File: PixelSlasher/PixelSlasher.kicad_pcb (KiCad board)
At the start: 2 copper layers, 52.8 x 149.3 mm, 22 parts, among them J1 VGA Input, J2 CV Red, J3 CV Green, J4 CV Blue, Q1 BC337, Q2 BC337, Q3 BC337, SW1 SW_SPDT, SW2 SW_SPDT, SW3 SW_SPDT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

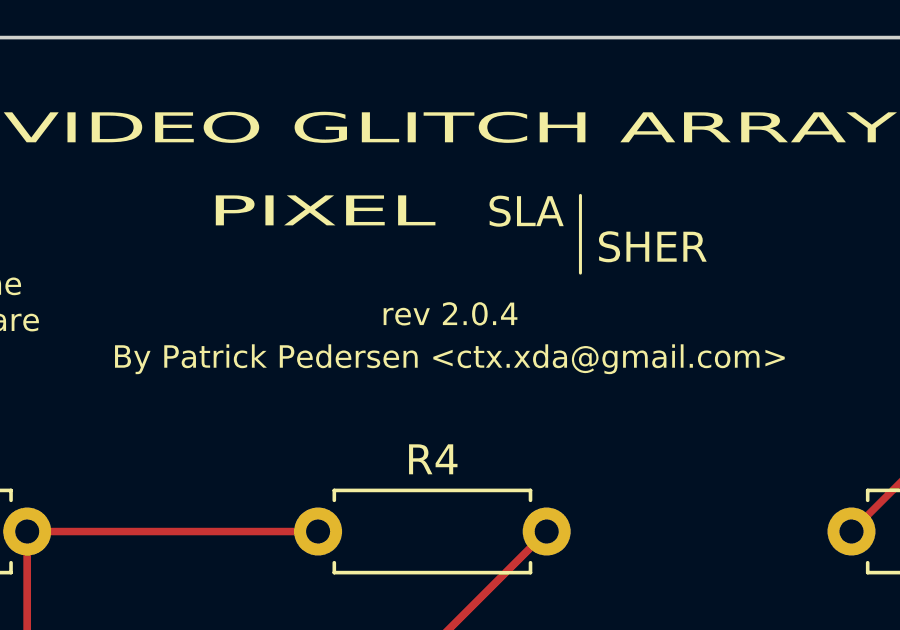
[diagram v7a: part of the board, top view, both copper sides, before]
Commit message: PixelSlasher: Rev 2.0.5: Ground slide pot case mounts
Signed-off-by: Patrick Pedersen <ctx.xda@gmail.com>
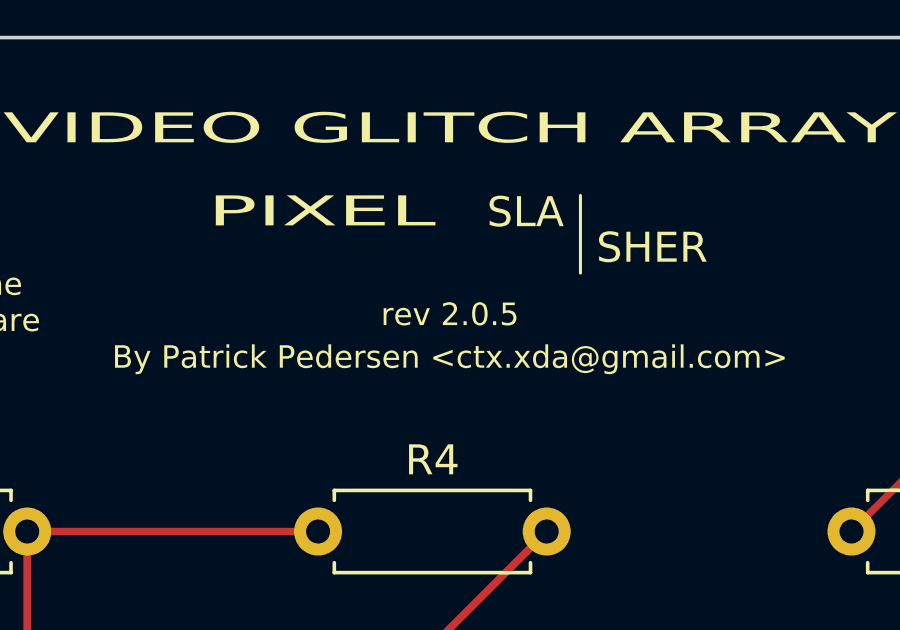
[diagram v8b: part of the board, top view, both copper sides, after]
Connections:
- RV1 pad MP: (no net) -> GND
- RV2 pad MP: (no net) -> GND
- RV3 pad MP: (no net) -> GND
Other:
- board text added: "rev 2.0.5"
- board text removed: "rev 2.0.4"
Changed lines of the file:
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@@
   (title_block
     (date 2019-08-30)
-    (rev 2.0.4)
+    (rev 2.0.5)
     (comment 2 https://www.tapr.org/ohl.html)
     (comment 3 "License: TAPR Open Hardware License v1.0")
@@
     (mod_text_size 1 1)
     (mod_text_width 0.15)
-    (pad_size 1.524 1.524)
-    (pad_drill 0.762)
+    (pad_size 2.7 2.7)
+    (pad_drill 1.7)
     (pad_to_mask_clearance 0.051)
     (solder_mask_min_width 0.25)
@@
       (effects (font (size 1 1) (thickness 0.15)))
     )
+    (fp_text user %R (at 29.25 1.75 90) (layer F.Fab)
+      (effects (font (size 1 1) (thickness 0.15)))
+    )
+    (fp_line (start 59.75 -3.25) (end -1.25 -3.25) (layer F.CrtYd) (width 0.05))
+    (fp_line (start 59.75 6.75) (end 59.75 -3.25) (layer F.CrtYd) (width 0.05))
+    (fp_line (start -1.25 6.75) (end 59.75 6.75) (layer F.CrtYd) (width 0.05))
+    (fp_line (start -1.25 -3.25) (end -1.25 6.75) (layer F.CrtYd) (width 0.05))
+    (fp_line (start 51.75 1.75) (end 51 2.5) (layer F.SilkS) (width 0.12))
+    (fp_line (start 51 1) (end 51.75 1.75) (layer F.SilkS) (width 0.12))
+    (fp_line (start 51.75 0.25) (end 51.75 3.25) (layer F.SilkS) (width 0.12))
+    (fp_line (start 6.75 1.75) (end 7.5 2.5) (layer F.SilkS) (width 0.12))
+    (fp_line (start 7.5 1) (end 6.75 1.75) (layer F.SilkS) (width 0.12))
+    (fp_line (start 6.75 0.25) (end 6.75 3.25) (layer F.SilkS) (width 0.12))
+    (fp_line (start 6.75 1.75) (end 51.75 1.75) (layer F.SilkS) (width 0.12))
+    (fp_line (start -1.675 0.5) (end -1.175 0) (layer F.SilkS) (width 0.12))
+    (fp_line (start -1.675 -0.5) (end -1.675 0.5) (layer F.SilkS) (width 0.12))
+    (fp_line (start -1.175 0) (end -1.675 -0.5) (layer F.SilkS) (width 0.12))
+    (fp_line (start 59.37 0.823) (end 59.37 6.37) (layer F.SilkS) (width 0.12))
+    (fp_line (start 59.37 -2.87) (end 59.37 -0.823) (layer F.SilkS) (width 0.12))
+    (fp_line (start -0.87 4.323) (end -0.87 6.37) (layer F.SilkS) (width 0.12))
+    (fp_line (start -0.87 1.175) (end -0.87 2.678) (layer F.SilkS) (width 0.12))
+    (fp_line (start -0.87 -2.87) (end -0.87 -1.175) (layer F.SilkS) (width 0.12))
+    (fp_line (start 55.986 6.37) (end 59.37 6.37) (layer F.SilkS) (width 0.12))
+    (fp_line (start 5.786 6.37) (end 52.715 6.37) (layer F.SilkS) (width 0.12))
+    (fp_line (start -0.87 6.37) (end 2.515 6.37) (layer F.SilkS) (width 0.12))
+    (fp_line (start 54.786 -2.87) (end 59.37 -2.87) (layer F.SilkS) (width 0.12))
+    (fp_line (start 6.986 -2.87) (end 51.515 -2.87) (layer F.SilkS) (width 0.12))
+    (fp_line (start -0.87 -2.87) (end 3.715 -2.87) (layer F.SilkS) (width 0.12))
+    (fp_line (start -0.75 -1.75) (end 0.25 -2.75) (layer F.Fab) (width 0.1))
+    (fp_line (start -0.75 6.25) (end -0.75 -1.75) (layer F.Fab) (width 0.1))
+    (fp_line (start 59.25 6.25) (end -0.75 6.25) (layer F.Fab) (width 0.1))
+    (fp_line (start 59.25 -2.75) (end 59.25 6.25) (layer F.Fab) (width 0.1))
+    (fp_line (start 0.25 -2.75) (end 59.25 -2.75) (layer F.Fab) (width 0.1))
+    (fp_circle (center 57.25 1.75) (end 58.25 1.75) (layer F.Fab) (width 0.1))
     (fp_circle (center 1.25 1.75) (end 2.25 1.75) (layer F.Fab) (width 0.1))
-    (fp_circle (center 57.25 1.75) (end 58.25 1.75) (layer F.Fab) (width 0.1))
-    (fp_line (start 0.25 -2.75) (end 59.25 -2.75) (layer F.Fab) (width 0.1))
-    (fp_line (start 59.25 -2.75) (end 59.25 6.25) (layer F.Fab) (width 0.1))
-    (fp_line (start 59.25 6.25) (end -0.75 6.25) (layer F.Fab) (width 0.1))
-    (fp_line (start -0.75 6.25) (end -0.75 -1.75) (layer F.Fab) (width 0.1))
-    (fp_line (start -0.75 -1.75) (end 0.25 -2.75) (layer F.Fab) (width 0.1))
-    (fp_line (start -0.87 -2.87) (end 3.715 -2.87) (layer F.SilkS) (width 0.12))
-    (fp_line (start 6.986 -2.87) (end 51.515 -2.87) (layer F.SilkS) (width 0.12))
-    (fp_line (start 54.786 -2.87) (end 59.37 -2.87) (layer F.SilkS) (width 0.12))
-    (fp_line (start -0.87 6.37) (end 2.515 6.37) (layer F.SilkS) (width 0.12))
-    (fp_line (start 5.786 6.37) (end 52.715 6.37) (layer F.SilkS) (width 0.12))
-    (fp_line (start 55.986 6.37) (end 59.37 6.37) (layer F.SilkS) (width 0.12))
-    (fp_line (start -0.87 -2.87) (end -0.87 -1.175) (layer F.SilkS) (width 0.12))
-    (fp_line (start -0.87 1.175) (end -0.87 2.678) (layer F.SilkS) (width 0.12))
-    (fp_line (start -0.87 4.323) (end -0.87 6.37) (layer F.SilkS) (width 0.12))
-    (fp_line (start 59.37 -2.87) (end 59.37 -0.823) (layer F.SilkS) (width 0.12))
-    (fp_line (start 59.37 0.823) (end 59.37 6.37) (layer F.SilkS) (width 0.12))
-    (fp_line (start -1.175 0) (end -1.675 -0.5) (layer F.SilkS) (width 0.12))
-    (fp_line (start -1.675 -0.5) (end -1.675 0.5) (layer F.SilkS) (width 0.12))
-    (fp_line (start -1.675 0.5) (end -1.175 0) (layer F.SilkS) (width 0.12))
-    (fp_line (start 6.75 1.75) (end 51.75 1.75) (layer F.SilkS) (width 0.12))
-    (fp_line (start 6.75 0.25) (end 6.75 3.25) (layer F.SilkS) (width 0.12))
-    (fp_line (start 7.5 1) (end 6.75 1.75) (layer F.SilkS) (width 0.12))
-    (fp_line (start 6.75 1.75) (end 7.5 2.5) (layer F.SilkS) (width 0.12))
-    (fp_line (start 51.75 0.25) (end 51.75 3.25) (layer F.SilkS) (width 0.12))
-    (fp_line (start 51 1) (end 51.75 1.75) (layer F.SilkS) (width 0.12))
-    (fp_line (start 51.75 1.75) (end 51 2.5) (layer F.SilkS) (width 0.12))
-    (fp_line (start -1.25 -3.25) (end -1.25 6.75) (layer F.CrtYd) (width 0.05))
-    (fp_line (start -1.25 6.75) (end 59.75 6.75) (layer F.CrtYd) (width 0.05))
-    (fp_line (start 59.75 6.75) (end 59.75 -3.25) (layer F.CrtYd) (width 0.05))
-    (fp_line (start 59.75 -3.25) (end -1.25 -3.25) (layer F.CrtYd) (width 0.05))
-    (fp_text user %R (at 29.25 1.75 90) (layer F.Fab)
-      (effects (font (size 1 1) (thickness 0.15)))
-    )
+    (pad MP thru_hole circle (at 54.35 5.95 90) (size 2.7 2.7) (drill 1.7) (layers *.Cu *.Mask)
+      (net 4 GND))
+    (pad MP thru_hole circle (at 4.15 5.95 90) (size 2.7 2.7) (drill 1.7) (layers *.Cu *.Mask)
+      (net 4 GND))
+    (pad MP thru_hole circle (at 53.15 -2.45 90) (size 2.7 2.7) (drill 1.7) (layers *.Cu *.Mask)
+      (net 4 GND))
+    (pad MP thru_hole circle (at 5.35 -2.45 90) (size 2.7 2.7) (drill 1.7) (layers *.Cu *.Mask)
+      (net 4 GND))
+    (pad 3 thru_hole circle (at 58.5 0 90) (size 1.75 1.75) (drill 1.2) (layers *.Cu *.Mask)
+      (net 4 GND))
+    (pad 2 thru_hole circle (at 0 3.5 90) (size 1.75 1.75) (drill 1.2) (layers *.Cu *.Mask)
+      (net 12 "Net-(RV1-Pad2)"))
     (pad 1 thru_hole rect (at 0 0 90) (size 1.75 1.75) (drill 1.2) (layers *.Cu *.Mask)
       (net 9 "Net-(R1-Pad2)"))
-    (pad 2 thru_hole circle (at 0 3.5 90) (size 1.75 1.75) (drill 1.2) (layers *.Cu *.Mask)
-      (net 12 "Net-(RV1-Pad2)"))
-    (pad 3 thru_hole circle (at 58.5 0 90) (size 1.75 1.75) (drill 1.2) (layers *.Cu *.Mask)
-      (net 4 GND))
-    (pad MP thru_hole circle (at 5.35 -2.45 90) (size 2.7 2.7) (drill 1.7) (layers *.Cu *.Mask))
-    (pad MP thru_hole circle (at 53.15 -2.45 90) (size 2.7 2.7) (drill 1.7) (layers *.Cu *.Mask))
-    (pad MP thru_hole circle (at 4.15 5.95 90) (size 2.7 2.7) (drill 1.7) (layers *.Cu *.Mask))
-    (pad MP thru_hole circle (at 54.35 5.95 90) (size 2.7 2.7) (drill 1.7) (layers *.Cu *.Mask))
     (model ${KISYS3DMOD}/Potentiometer_THT.3dshapes/Potentiometer_Bourns_PTA4543_Single_Slide.wrl
       (at (xyz 0 0 0))
@@
     (pad 3 thru_hole circle (at 58.5 0 90) (size 1.75 1.75) (drill 1.2) (layers *.Cu *.Mask)
       (net 4 GND))
-    (pad MP thru_hole circle (at 5.35 -2.45 90) (size 2.7 2.7) (drill 1.7) (layers *.Cu *.Mask))
-    (pad MP thru_hole circle (at 53.15 -2.45 90) (size 2.7 2.7) (drill 1.7) (layers *.Cu *.Mask))
-    (pad MP thru_hole circle (at 4.15 5.95 90) (size 2.7 2.7) (drill 1.7) (layers *.Cu *.Mask))
-    (pad MP thru_hole circle (at 54.35 5.95 90) (size 2.7 2.7) (drill 1.7) (layers *.Cu *.Mask))
+    (pad MP thru_hole circle (at 5.35 -2.45 90) (size 2.7 2.7) (drill 1.7) (layers *.Cu *.Mask)
+      (net 4 GND))
+    (pad MP thru_hole circle (at 53.15 -2.45 90) (size 2.7 2.7) (drill 1.7) (layers *.Cu *.Mask)
+      (net 4 GND))
+    (pad MP thru_hole circle (at 4.15 5.95 90) (size 2.7 2.7) (drill 1.7) (layers *.Cu *.Mask)
+      (net 4 GND))
+    (pad MP thru_hole circle (at 54.35 5.95 90) (size 2.7 2.7) (drill 1.7) (layers *.Cu *.Mask)
+      (net 4 GND))
     (model ${KISYS3DMOD}/Potentiometer_THT.3dshapes/Potentiometer_Bourns_PTA4543_Single_Slide.wrl
       (at (xyz 0 0 0))
@@
     (fp_circle (center 57.25 1.75) (end 58.25 1.75) (layer F.Fab) (width 0.1))
     (fp_circle (center 1.25 1.75) (end 2.25 1.75) (layer F.Fab) (width 0.1))
-    (pad MP thru_hole circle (at 54.35 5.95 90) (size 2.7 2.7) (drill 1.7) (layers *.Cu *.Mask))
-    (pad MP thru_hole circle (at 4.15 5.95 90) (size 2.7 2.7) (drill 1.7) (layers *.Cu *.Mask))
-    (pad MP thru_hole circle (at 53.15 -2.45 90) (size 2.7 2.7) (drill 1.7) (layers *.Cu *.Mask))
-    (pad MP thru_hole circle (at 5.35 -2.45 90) (size 2.7 2.7) (drill 1.7) (layers *.Cu *.Mask))
+    (pad MP thru_hole circle (at 54.35 5.95 90) (size 2.7 2.7) (drill 1.7) (layers *.Cu *.Mask)
+      (net 4 GND))
+    (pad MP thru_hole circle (at 4.15 5.95 90) (size 2.7 2.7) (drill 1.7) (layers *.Cu *.Mask)
+      (net 4 GND))
+    (pad MP thru_hole circle (at 53.15 -2.45 90) (size 2.7 2.7) (drill 1.7) (layers *.Cu *.Mask)
+      (net 4 GND))
+    (pad MP thru_hole circle (at 5.35 -2.45 90) (size 2.7 2.7) (drill 1.7) (layers *.Cu *.Mask)
+      (net 4 GND))
     (pad 3 thru_hole circle (at 58.5 0 90) (size 1.75 1.75) (drill 1.2) (layers *.Cu *.Mask)
       (net 4 GND))
@@
   (gr_circle (center 111.42 38.5826) (end 112.17 38.5826) (layer Edge.Cuts) (width 0.12))
   (gr_circle (center 149.9108 38.5826) (end 150.6608 38.5826) (layer Edge.Cuts) (width 0.12))
-  (gr_text "rev 2.0.4" (at 130.6068 42.30116) (layer F.SilkS)
+  (gr_text "rev 2.0.5" (at 130.6068 42.30116) (layer F.SilkS)
     (effects (font (size 0.75 0.75) (thickness 0.1)))
   )
